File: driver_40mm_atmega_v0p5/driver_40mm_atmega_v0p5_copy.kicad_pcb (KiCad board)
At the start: 6 copper layers, 40.4 x 40.4 mm, 424 parts, among them IC1 ATMEGA328P-M, IC2 ATMEGA328P-M, IC3 ATMEGA328P-M, IC4 ATMEGA328P-M, P1 CONN_2X2, P2 CONN_2X2, P3 CONN_2X2, P4 CONN_2X2, Q1 NMOS, Q10 NMOS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

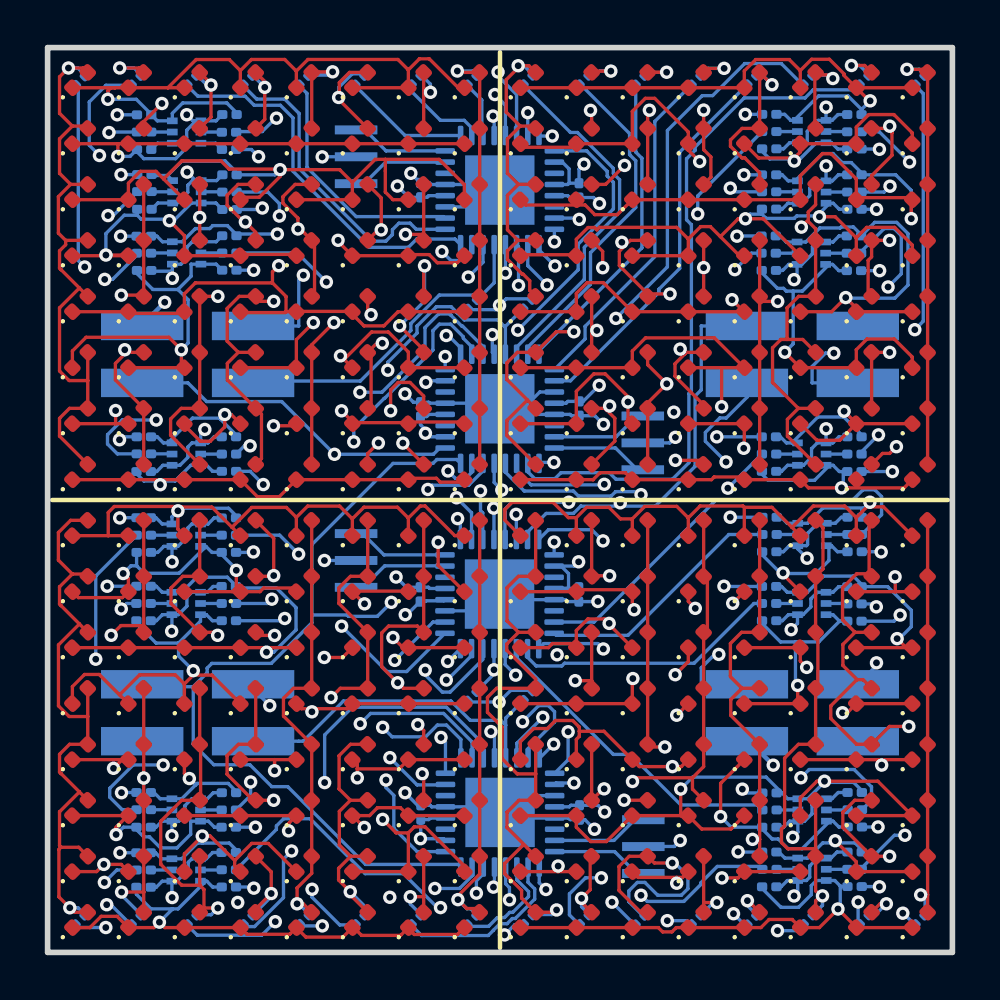
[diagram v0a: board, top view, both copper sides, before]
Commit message: Added design files for new v0.5 driver design.
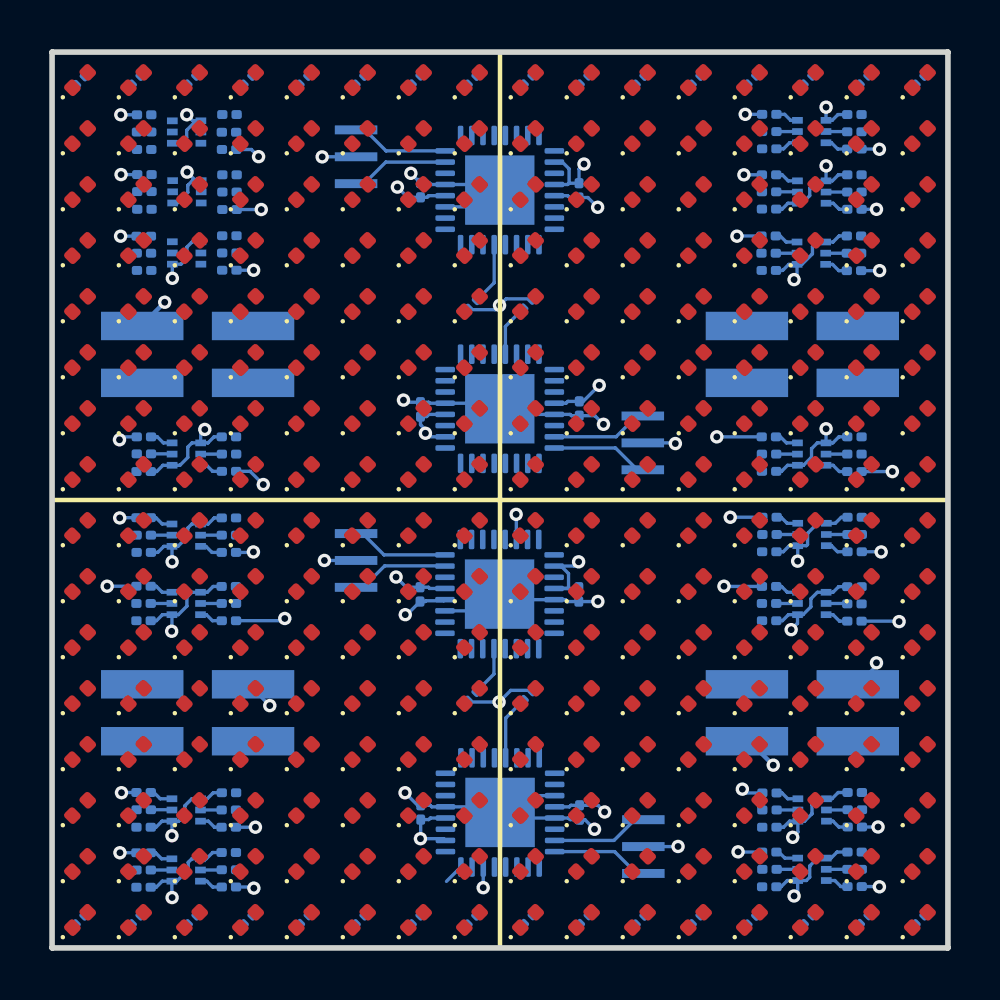
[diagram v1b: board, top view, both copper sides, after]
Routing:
- net /MISO: track 79.5 -> 1.12 mm, vias 3 -> 0
- net /MOSI: track 77.2 -> 0.00 mm, vias 4 -> 0
- net /SCK: track 70.1 -> 0.00 mm, vias 4 -> 0
- net /COL3_DRV3: track 41.7 -> 0.00 mm, vias 3 -> 0
- net /ROW4_DRV2: track 40.9 -> 0.00 mm, vias 2 -> 0
- net Net-(D129-A): track 39.6 -> 0.00 mm, vias 2 -> 0
- net /ROW7_DRV3: track 38.6 -> 0.00 mm, vias 2 -> 0
- net /ROW6_INV1: track 39.6 -> 1.06 mm, vias 3 -> 0
- net /ROW5_INV0: track 38.5 -> 0.00 mm, vias 3 -> 0
- net /ROW4_INV2: track 39.3 -> 1.06 mm, vias 2 -> 0
- net /ROW2_INV0: track 37.4 -> 0.00 mm, vias 1 -> 0
- net /ROW3_DRV2: track 37.3 -> 0.00 mm, vias 3 -> 0
- net /ROW2_INV3: track 38.2 -> 1.06 mm, vias 4 -> 0
- net /ROW4_INV3: track 37.7 -> 1.05 mm, vias 3 -> 0
- net Net-(D81-A): track 35.1 -> 0.00 mm, vias 2 -> 0
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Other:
- board size 40.4 x 40.4 mm -> 40 x 40 mm
- board text removed: "Panels G4 Driver V0.5 R1"
